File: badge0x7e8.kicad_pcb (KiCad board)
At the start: 2 copper layers, 66 x 55 mm, 18 parts, among them Q1 Q_NPN_BEC, SW1 SW_SPDT

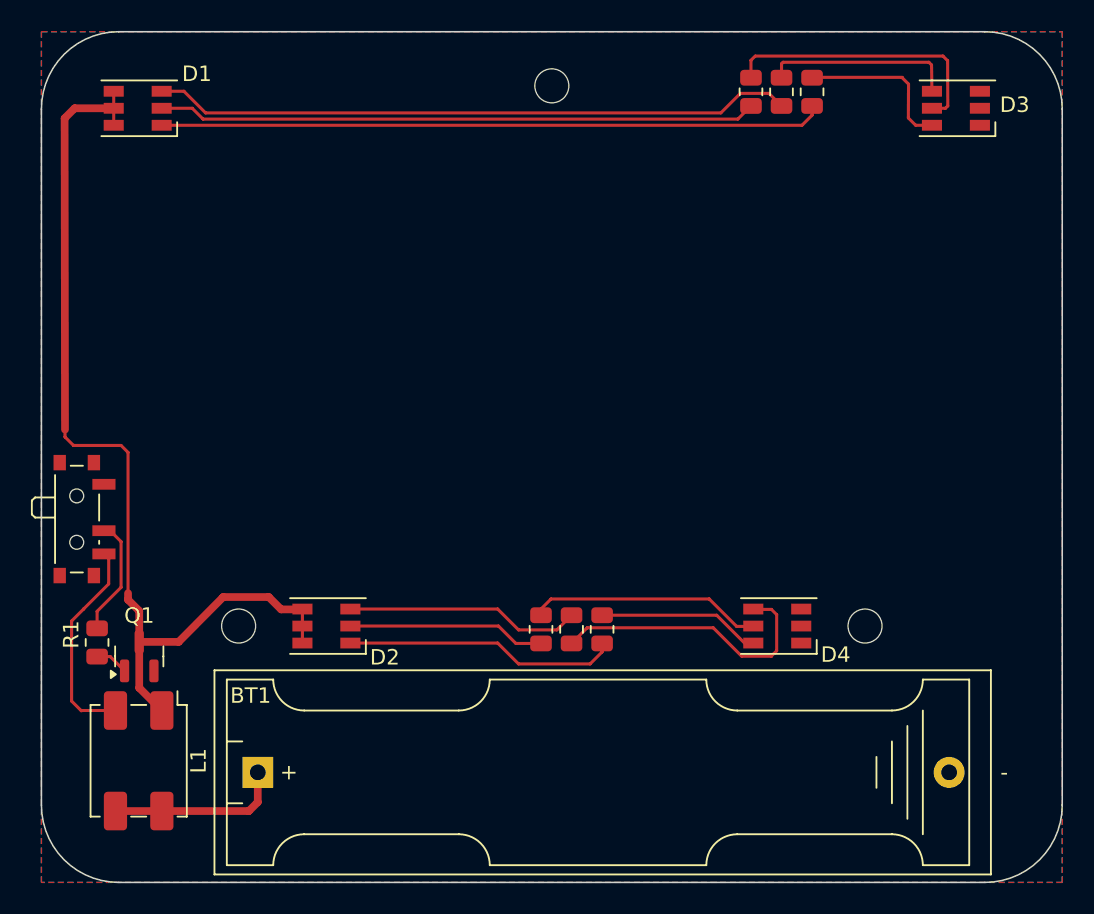
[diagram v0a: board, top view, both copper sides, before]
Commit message: round tracks are nice
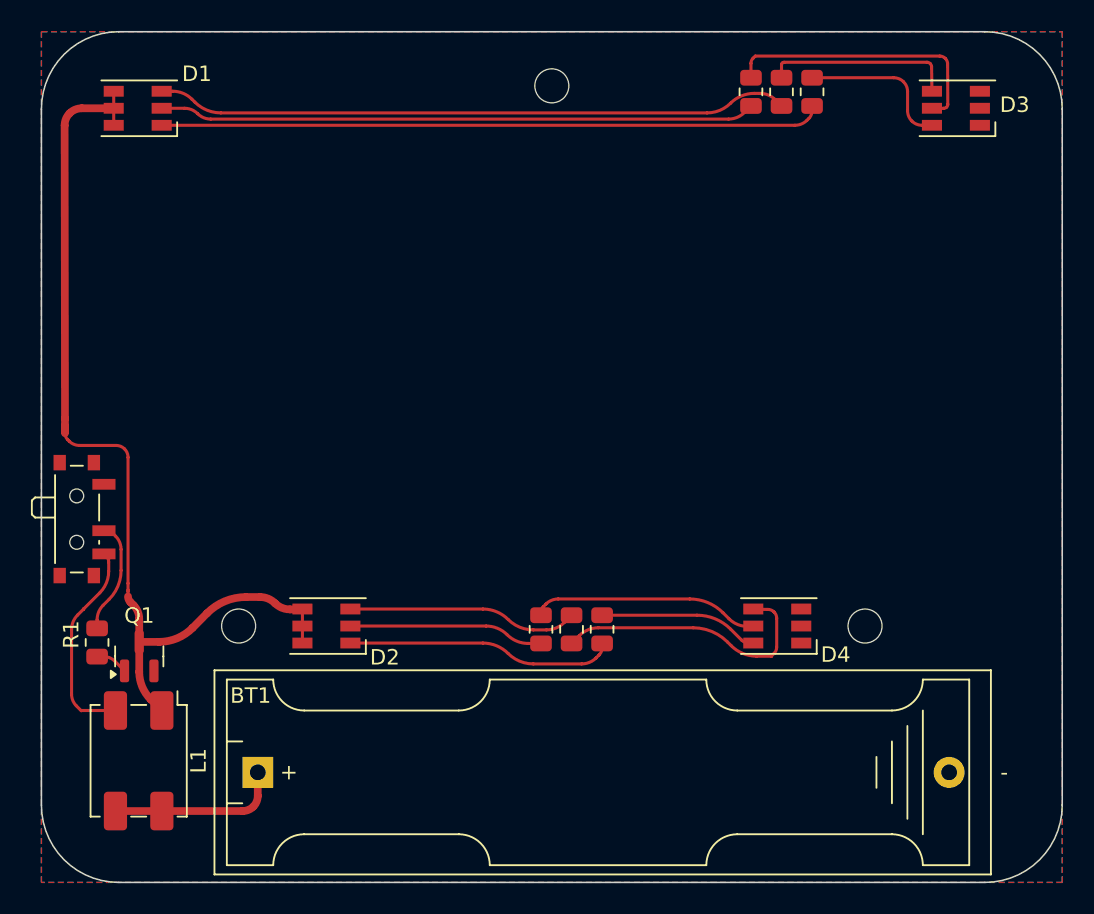
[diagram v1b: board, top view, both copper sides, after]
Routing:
- net Net-(D1-AB): track 62.6 -> 61.7 mm
- net Net-(SW1-C): track 14.2 -> 13.5 mm
